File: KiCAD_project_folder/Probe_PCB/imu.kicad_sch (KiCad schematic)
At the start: 3 parts, among them U2 BMI160

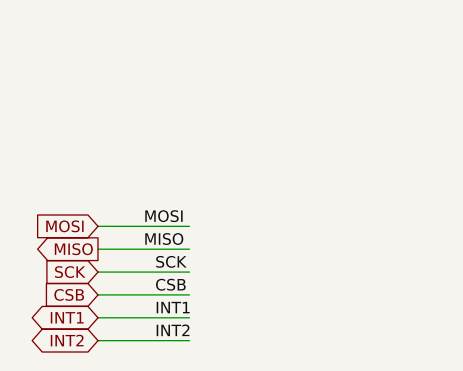
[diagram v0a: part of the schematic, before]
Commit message: added new squeletton for probe pcb
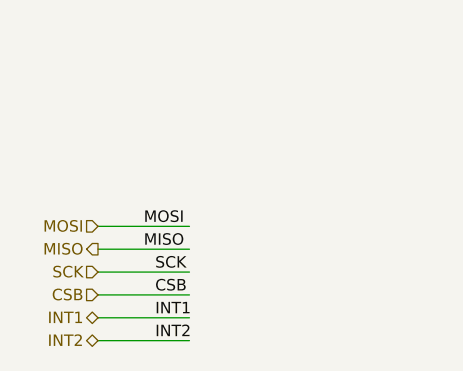
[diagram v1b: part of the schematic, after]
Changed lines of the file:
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@@
     (effects (font (size 1.27 1.27)) (justify left bottom))
   )
-  (global_label "CSB" (shape input) (at 43.18 78.74 180) (fields_autoplaced)
+  (hierarchical_label "CSB" (shape input) (at 43.18 78.74 180) (fields_autoplaced)
     (effects (font (size 1.27 1.27)) (justify right))
-    (property "Intersheetrefs" "${INTERSHEET_REFS}" (at 36.5247 78.74 0)
-      (effects (font (size 1.27 1.27)) (justify right) hide)
-    )
   )
-  (global_label "INT2" (shape bidirectional) (at 43.18 83.82 180) (fields_autoplaced)
+  (hierarchical_label "SCK" (shape input) (at 43.18 76.2 180) (fields_autoplaced)
     (effects (font (size 1.27 1.27)) (justify right))
-    (property "Intersheetrefs" "${INTERSHEET_REFS}" (at 35.0505 83.82 0)
-      (effects (font (size 1.27 1.27)) (justify right) hide)
-    )
   )
-  (global_label "MISO" (shape output) (at 43.18 73.66 180) (fields_autoplaced)
+  (hierarchical_label "INT2" (shape bidirectional) (at 43.18 83.82 180) (fields_autoplaced)
     (effects (font (size 1.27 1.27)) (justify right))
-    (property "Intersheetrefs" "${INTERSHEET_REFS}" (at 35.678 73.66 0)
-      (effects (font (size 1.27 1.27)) (justify right) hide)
-    )
   )
-  (global_label "INT1" (shape bidirectional) (at 43.18 81.28 180) (fields_autoplaced)
+  (hierarchical_label "INT1" (shape bidirectional) (at 43.18 81.28 180) (fields_autoplaced)
     (effects (font (size 1.27 1.27)) (justify right))
-    (property "Intersheetrefs" "${INTERSHEET_REFS}" (at 35.0505 81.28 0)
-      (effects (font (size 1.27 1.27)) (justify right) hide)
-    )
   )
-  (global_label "MOSI" (shape input) (at 43.18 71.12 180) (fields_autoplaced)
+  (hierarchical_label "MOSI" (shape input) (at 43.18 71.12 180) (fields_autoplaced)
     (effects (font (size 1.27 1.27)) (justify right))
-    (property "Intersheetrefs" "${INTERSHEET_REFS}" (at 35.678 71.12 0)
-      (effects (font (size 1.27 1.27)) (justify right) hide)
-    )
   )
-  (global_label "SCK" (shape input) (at 43.18 76.2 180) (fields_autoplaced)
+  (hierarchical_label "MISO" (shape output) (at 43.18 73.66 180) (fields_autoplaced)
     (effects (font (size 1.27 1.27)) (justify right))
-    (property "Intersheetrefs" "${INTERSHEET_REFS}" (at 36.5247 76.2 0)
-      (effects (font (size 1.27 1.27)) (justify right) hide)
-    )
   )
   (symbol (lib_id "power:VDD") (at 167.64 62.23 0) (unit 1)
